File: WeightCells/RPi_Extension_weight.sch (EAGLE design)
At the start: 29 parts, among them U1 AD7730BRUZ, U2 AD7730BRUZ, U3 AD7730BRUZ, U4 AD7730BRUZ, U5 AD7730BRUZ, U6 AD7730BRUZ, U7 AD7730BRUZ, U8 AD7730BRUZ, U9 STM32F103RCT6

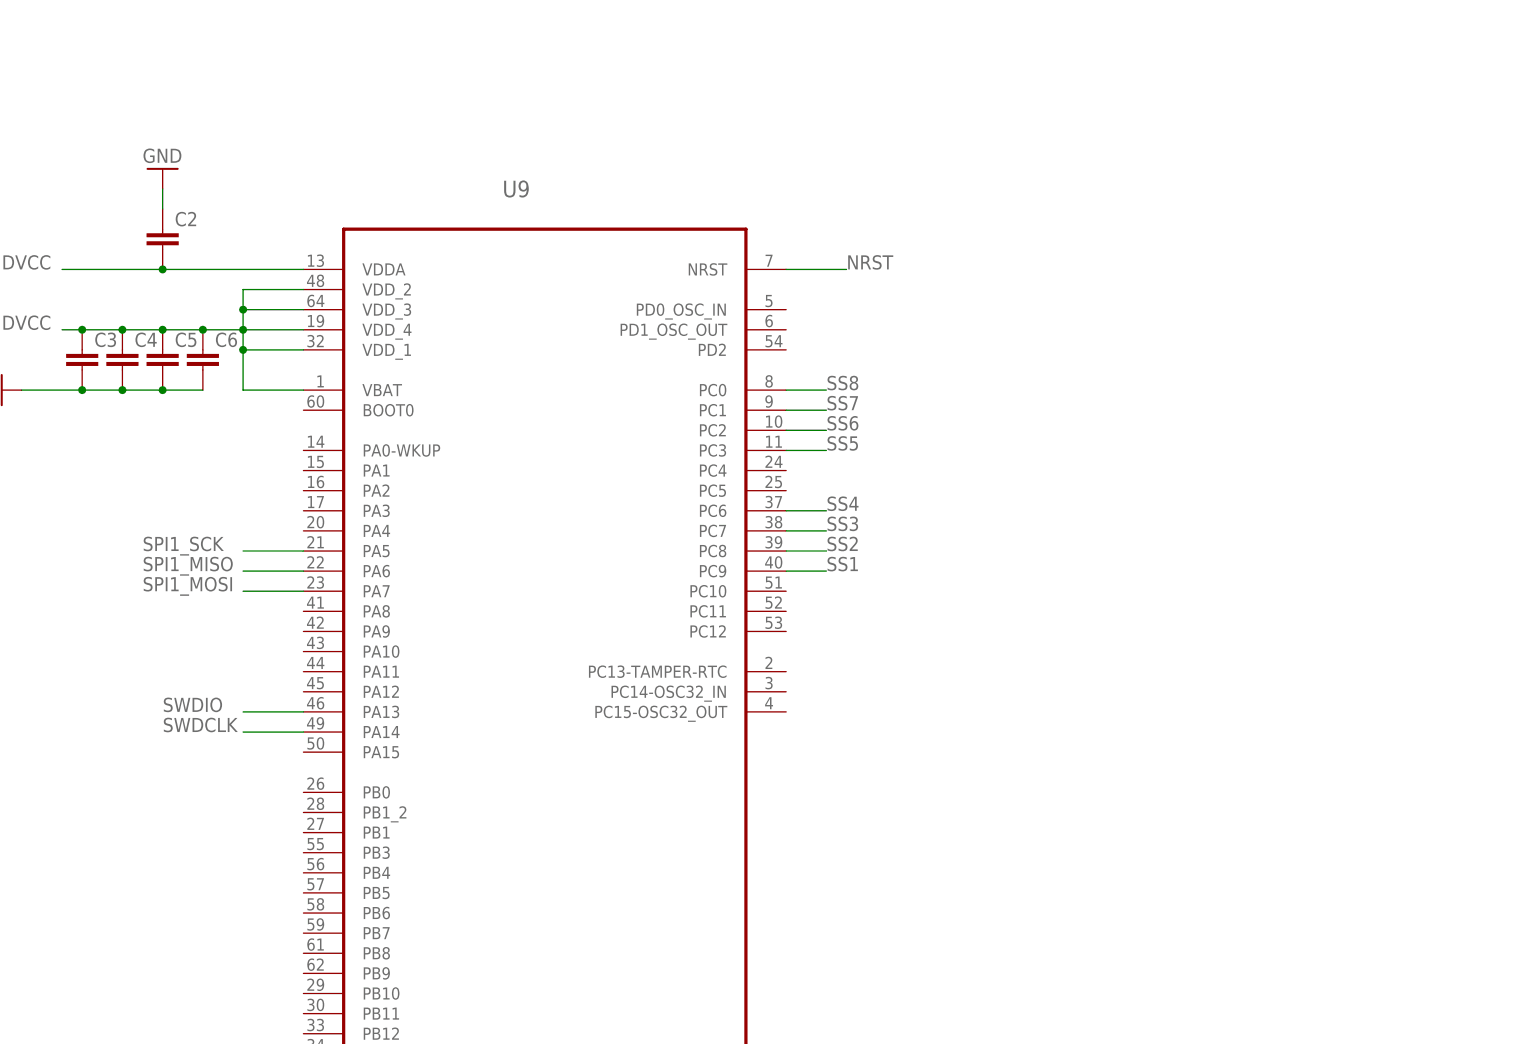
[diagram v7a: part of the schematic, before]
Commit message: added crystal and revisited layout
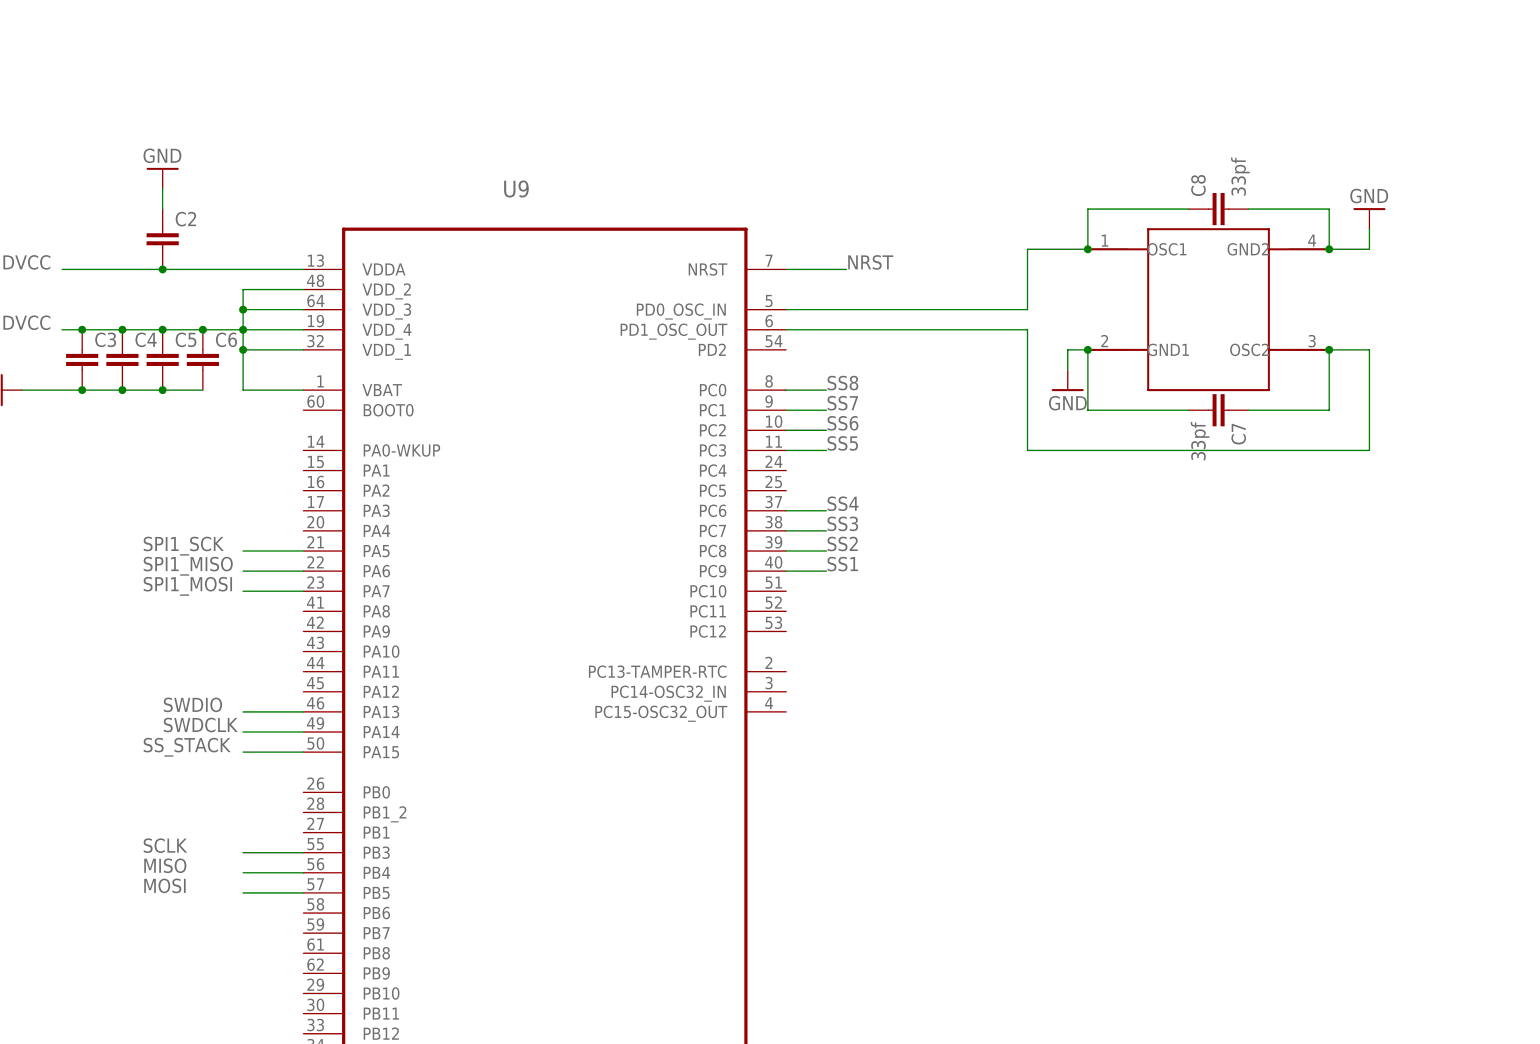
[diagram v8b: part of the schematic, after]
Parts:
- added C7, C8: 33pf, rcl:C-EUC0603
- added U$2: ABM3B, ABM3B:ABM3B
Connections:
- new net N$2: C8.1, U$2.OSC1, U9.PD0_OSC_IN
- new net N$3: C7.1, U$2.OSC2, U9.PD1_OSC_OUT
- net GND: now also C7.2, C8.2, U$2.GND1, U$2.GND2
- net MISO: now also U9.PB4
- net MOSI: now also U9.PB5
- net SCLK: now also U9.PB3
- net SS_STACK: now also U9.PA15
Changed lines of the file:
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@@
 <part name="GND26" library="supply1" deviceset="GND" device=""/>
 <part name="P+17" library="supply1" deviceset="+5V" device=""/>
+<part name="U$2" library="ABM3B" deviceset="ABM3B" device=""/>
+<part name="GND27" library="supply1" deviceset="GND" device=""/>
+<part name="GND28" library="supply1" deviceset="GND" device=""/>
+<part name="C7" library="rcl" deviceset="C-EU" device="C0603" value="33pf"/>
+<part name="C8" library="rcl" deviceset="C-EU" device="C0603" value="33pf"/>
 </parts>
 <sheets>
@@
 <instance part="GND26" gate="1" x="139.7" y="73.66" rot="R270"/>
 <instance part="P+17" gate="1" x="144.78" y="66.04" rot="R180"/>
+<instance part="U$2" gate="G$1" x="266.7" y="15.24"/>
+<instance part="GND27" gate="1" x="287.02" y="27.94" rot="MR180"/>
+<instance part="GND28" gate="1" x="248.92" y="5.08" rot="MR0"/>
+<instance part="C7" gate="G$1" x="269.24" y="2.54" rot="R270"/>
+<instance part="C8" gate="G$1" x="266.7" y="27.94" rot="R90"/>
 </instances>
 <busses>
@@
 <wire x1="149.86" y1="73.66" x2="142.24" y2="73.66" width="0.1524" layer="91"/>
 <pinref part="GND26" gate="1" pin="GND"/>
+</segment>
+<segment>
+<pinref part="U$2" gate="G$1" pin="GND1"/>
+<pinref part="GND28" gate="1" pin="GND"/>
+<wire x1="251.46" y1="10.16" x2="248.92" y2="10.16" width="0.1524" layer="91"/>
+<wire x1="248.92" y1="10.16" x2="248.92" y2="7.62" width="0.1524" layer="91"/>
+<wire x1="251.46" y1="10.16" x2="251.46" y2="2.54" width="0.1524" layer="91"/>
+<junction x="251.46" y="10.16"/>
+<pinref part="C7" gate="G$1" pin="2"/>
+<wire x1="251.46" y1="2.54" x2="264.16" y2="2.54" width="0.1524" layer="91"/>
+</segment>
+<segment>
+<pinref part="U$2" gate="G$1" pin="GND2"/>
+<wire x1="281.94" y1="22.86" x2="287.02" y2="22.86" width="0.1524" layer="91"/>
+<pinref part="GND27" gate="1" pin="GND"/>
+<wire x1="287.02" y1="22.86" x2="287.02" y2="25.4" width="0.1524" layer="91"/>
+<pinref part="C8" gate="G$1" pin="2"/>
+<wire x1="271.78" y1="27.94" x2="281.94" y2="27.94" width="0.1524" layer="91"/>
+<wire x1="281.94" y1="27.94" x2="281.94" y2="22.86" width="0.1524" layer="91"/>
+<junction x="281.94" y="22.86"/>
 </segment>
 </net>
@@
 <label x="15.24" y="73.66" size="1.778" layer="95"/>
 </segment>
+<segment>
+<pinref part="U9" gate="A" pin="PB5"/>
+<wire x1="152.4" y1="-58.42" x2="144.78" y2="-58.42" width="0.1524" layer="91"/>
+<label x="132.08" y="-58.42" size="1.778" layer="95"/>
+</segment>
 </net>
 <net name="MISO" class="0">
@@
 <label x="15.24" y="71.12" size="1.778" layer="95"/>
 </segment>
+<segment>
+<pinref part="U9" gate="A" pin="PB4"/>
+<wire x1="152.4" y1="-55.88" x2="144.78" y2="-55.88" width="0.1524" layer="91"/>
+<label x="132.08" y="-55.88" size="1.778" layer="95"/>
+</segment>
 </net>
 <net name="SCLK" class="0">
@@
 <wire x1="15.24" y1="68.58" x2="7.62" y2="68.58" width="0.1524" layer="91"/>
 <label x="15.24" y="68.58" size="1.778" layer="95"/>
+</segment>
+<segment>
+<pinref part="U9" gate="A" pin="PB3"/>
+<wire x1="152.4" y1="-53.34" x2="144.78" y2="-53.34" width="0.1524" layer="91"/>
+<label x="132.08" y="-53.34" size="1.778" layer="95"/>
 </segment>
 </net>
@@
 <label x="15.24" y="30.48" size="1.778" layer="95"/>
 </segment>
+<segment>
+<pinref part="U9" gate="A" pin="PA15"/>
+<wire x1="152.4" y1="-40.64" x2="144.78" y2="-40.64" width="0.1524" layer="91"/>
+<label x="132.08" y="-40.64" size="1.778" layer="95"/>
+</segment>
 </net>
 <net name="U2_MCLK_OUT" class="0">
@@
 </segment>
 </net>
+<net name="N$2" class="0">
+<segment>
+<pinref part="U$2" gate="G$1" pin="OSC1"/>
+<wire x1="251.46" y1="22.86" x2="243.84" y2="22.86" width="0.1524" layer="91"/>
+<wire x1="243.84" y1="22.86" x2="243.84" y2="15.24" width="0.1524" layer="91"/>
+<pinref part="U9" gate="A" pin="PD0_OSC_IN"/>
+<wire x1="243.84" y1="15.24" x2="213.36" y2="15.24" width="0.1524" layer="91"/>
+<wire x1="251.46" y1="22.86" x2="251.46" y2="27.94" width="0.1524" layer="91"/>
+<junction x="251.46" y="22.86"/>
+<pinref part="C8" gate="G$1" pin="1"/>
+<wire x1="251.46" y1="27.94" x2="264.16" y2="27.94" width="0.1524" layer="91"/>
+</segment>
+</net>
+<net name="N$3" class="0">
+<segment>
+<pinref part="U$2" gate="G$1" pin="OSC2"/>
+<wire x1="281.94" y1="10.16" x2="287.02" y2="10.16" width="0.1524" layer="91"/>
+<wire x1="287.02" y1="10.16" x2="287.02" y2="-2.54" width="0.1524" layer="91"/>
+<wire x1="287.02" y1="-2.54" x2="243.84" y2="-2.54" width="0.1524" layer="91"/>
+<wire x1="243.84" y1="-2.54" x2="243.84" y2="12.7" width="0.1524" layer="91"/>
+<pinref part="U9" gate="A" pin="PD1_OSC_OUT"/>
+<wire x1="243.84" y1="12.7" x2="213.36" y2="12.7" width="0.1524" layer="91"/>
+<pinref part="C7" gate="G$1" pin="1"/>
+<wire x1="271.78" y1="2.54" x2="281.94" y2="2.54" width="0.1524" layer="91"/>
+<wire x1="281.94" y1="2.54" x2="281.94" y2="10.16" width="0.1524" layer="91"/>
+<junction x="281.94" y="10.16"/>
+</segment>
+</net>
